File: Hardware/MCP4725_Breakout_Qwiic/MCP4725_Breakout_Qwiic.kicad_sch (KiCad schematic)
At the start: 24 parts, among them J1 Conn_01x02, J2 I2C, J3 Qwiic_RA, J4 Qwiic_RA, U2 MCP4725

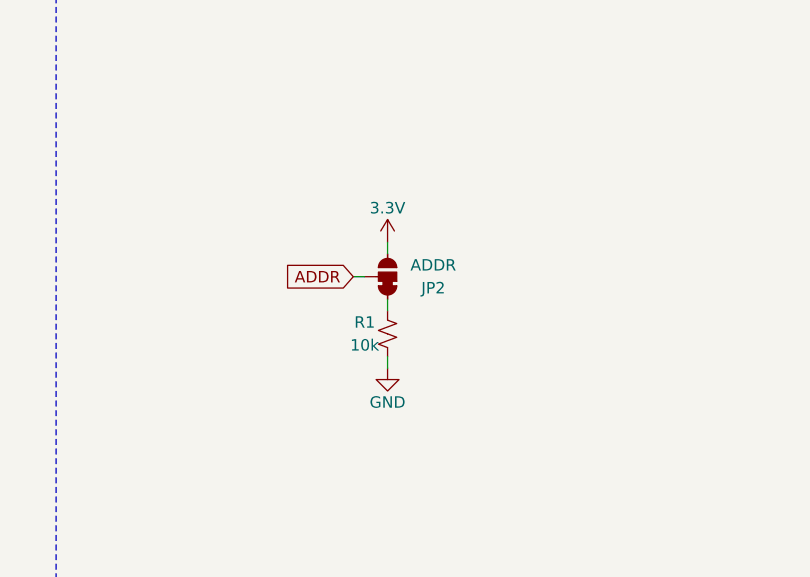
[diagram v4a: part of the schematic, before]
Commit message: Changes dual to single jumper
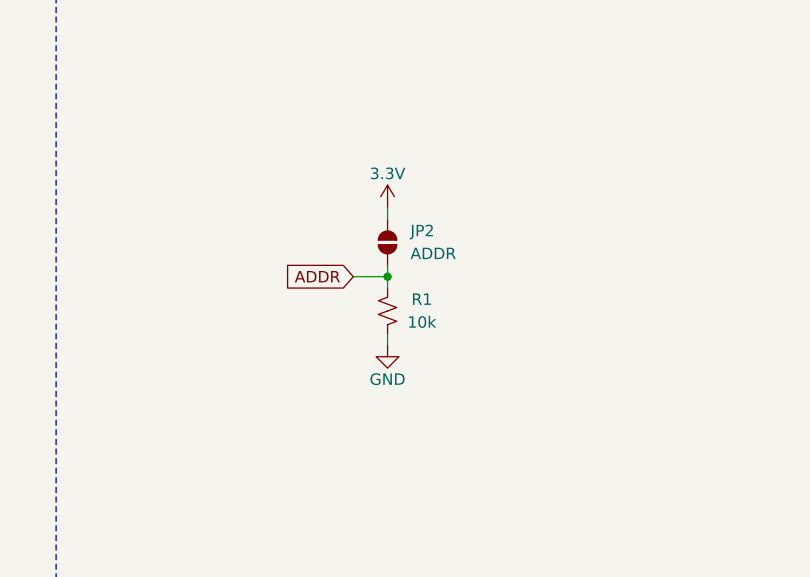
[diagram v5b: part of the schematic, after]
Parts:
- removed JP2: ADDR, SparkFun-Jumper:Jumper_3_NC-1_Trace, symbol SparkFun-Jumper:SolderJumper_3_Bridged12
- added JP2: ADDR, SparkFun-Jumper:Jumper_2_NO, symbol SparkFun-Jumper:SolderJumper_2_Open
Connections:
- net 3.3V: now also JP2.2 (B)
- net ADDR: now also R1.2, JP2.1 (A)
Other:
- moved on the sheet: R1
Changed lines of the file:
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@@
+	)
+	(junction
+		(at 139.7 132.08)
+		(diameter 0)
+		(color 0 0 0 0)
 	)
 	(junction
@@
 	(wire
 		(pts
-			(xy 135.89 132.08) (xy 137.16 132.08)
+			(xy 135.89 132.08) (xy 139.7 132.08)
 		)
 		(stroke
@@
 	(wire
 		(pts
-			(xy 139.7 128.27) (xy 139.7 129.54)
+			(xy 139.7 124.46) (xy 139.7 125.73)
 		)
 		(stroke
@@
 	(wire
 		(pts
-			(xy 139.7 142.24) (xy 139.7 140.97)
+			(xy 139.7 139.7) (xy 139.7 138.43)
 		)
 		(stroke
@@
 	(wire
 		(pts
-			(xy 139.7 134.62) (xy 139.7 135.89)
+			(xy 139.7 132.08) (xy 139.7 133.35)
+		)
+		(stroke
+			(width 0)
+			(type default)
+		)
+	)
+	(wire
+		(pts
+			(xy 139.7 130.81) (xy 139.7 132.08)
 		)
 		(stroke
@@
 		(row_heights 2.54 2.54 2.54 0 0 0 0 0 0 0 0)
 		(cells
-			(table_cell "Pin"
+			(table_cell "ADDR"
 				(exclude_from_sim no)
 				(at 124.46 102.87 0)
@@
 				)
 			)
-			(table_cell "GND"
+			(table_cell "Open"
 				(exclude_from_sim no)
 				(at 124.46 105.41 0)
@@
 				)
 			)
-			(table_cell "VDD"
+			(table_cell "Closed"
 				(exclude_from_sim no)
 				(at 124.46 107.95 0)
@@
 	)
 	(symbol
-		(lib_id "SparkFun-Jumper:SolderJumper_3_Bridged12")
-		(at 139.7 132.08 270)
-		(mirror x)
-		(unit 1)
-		(exclude_from_sim no)
-		(in_bom yes)
-		(on_board yes)
-		(dnp no)
-		(property "Reference" "JP2"
-			(at 144.78 133.35 90)
-			(effects
-				(font
-					(size 1.27 1.27)
-				)
-			)
-		)
-		(property "Value" "ADDR"
-			(at 144.78 130.81 90)
-			(effects
-				(font
-					(size 1.27 1.27)
-				)
-			)
-		)
-		(property "Footprint" "SparkFun-Jumper:Jumper_3_NC-1_Trace"
-			(at 134.62 132.08 0)
-			(effects
-				(font
-					(size 1.27 1.27)
-				)
-				(hide yes)
-			)
-		)
-		(property "Datasheet" "~"
-			(at 132.08 132.08 0)
-			(effects
-				(font
-					(size 1.27 1.27)
-				)
-				(hide yes)
-			)
-		)
-		(property "Description" "3-pole Solder Jumper, pins 1+2 closed/bridged"
-			(at 129.54 132.08 0)
-			(effects
-				(font
-					(size 1.27 1.27)
-				)
-				(hide yes)
-			)
-		)
-		(pin "2"
-		)
-		(pin "1"
-		)
-		(pin "3"
-		)
-		(instances
-			(project ""
-				(path "/bf35e96c-ec8b-4540-83a4-3cc6df170383"
-					(reference "JP2")
-					(unit 1)
-				)
-			)
-		)
-	)
-	(symbol
 		(lib_id "SparkFun-Aesthetic:Fiducial_0.5mm")
 		(at 278.13 175.26 0)
@@
 	)
 	(symbol
+		(lib_id "SparkFun-Jumper:SolderJumper_2_Open")
+		(at 139.7 128.27 90)
+		(unit 1)
+		(exclude_from_sim no)
+		(in_bom yes)
+		(on_board yes)
+		(dnp no)
+		(fields_autoplaced yes)
+		(property "Reference" "JP2"
+			(at 142.24 126.9999 90)
+			(effects
+				(font
+					(size 1.27 1.27)
+				)
+				(justify right)
+			)
+		)
+		(property "Value" "ADDR"
+			(at 142.24 129.5399 90)
+			(effects
+				(font
+					(size 1.27 1.27)
+				)
+				(justify right)
+			)
+		)
+		(property "Footprint" "SparkFun-Jumper:Jumper_2_NO"
+			(at 143.002 128.27 0)
+			(effects
+				(font
+					(size 1.27 1.27)
+				)
+				(hide yes)
+			)
+		)
+		(property "Datasheet" "~"
+			(at 146.05 128.27 0)
+			(effects
+				(font
+					(size 1.27 1.27)
+				)
+				(hide yes)
+			)
+		)
+		(property "Description" "Solder Jumper, 2-pole, open"
+			(at 148.59 128.27 0)
+			(effects
+				(font
+					(size 1.27 1.27)
+				)
+				(hide yes)
+			)
+		)
+		(pin "2"
+		)
+		(pin "1"
+		)
+		(instances
+			(project ""
+				(path "/bf35e96c-ec8b-4540-83a4-3cc6df170383"
+					(reference "JP2")
+					(unit 1)
+				)
+			)
+		)
+	)
+	(symbol
 		(lib_id "SparkFun-Resistor:10k_0603")
-		(at 139.7 138.43 90)
+		(at 139.7 135.89 270)
+		(mirror x)
 		(unit 1)
 		(exclude_from_sim no)
@@
 		(dnp no)
 		(property "Reference" "R1"
-			(at 137.16 137.16 90)
+			(at 143.51 134.62 90)
 			(effects
 				(font
@@
 		)
 		(property "Value" "10k"
-			(at 137.16 139.7 90)
+			(at 143.51 137.16 90)
 			(effects
 				(font
@@
 		)
 		(property "Footprint" "SparkFun-Resistor:R_0603_1608Metric"
-			(at 144.018 138.43 0)
+			(at 135.382 135.89 0)
 			(effects
 				(font
@@
 		)
 		(property "Datasheet" "https://www.vishay.com/docs/20035/dcrcwe3.pdf"
-			(at 148.59 138.43 0)
+			(at 130.81 135.89 0)
 			(effects
 				(font
@@
 		)
 		(property "Description" "Resistor"
-			(at 151.13 138.43 0)
+			(at 128.27 135.89 0)
 			(effects
 				(font
@@
 		)
 		(property "PROD_ID" "RES-00824"
-			(at 146.05 138.43 0)
+			(at 133.35 135.89 0)
 			(effects
 				(font
@@
 	(symbol
 		(lib_id "SparkFun-PowerSymbol:GND")
-		(at 139.7 142.24 0)
+		(at 139.7 139.7 0)
 		(unit 1)
 		(exclude_from_sim no)
@@
 		(fields_autoplaced yes)
 		(property "Reference" "#PWR02"
+			(at 139.7 146.05 0)
+			(effects
+				(font
+					(size 1.27 1.27)
+				)
+				(hide yes)
+			)
+		)
+		(property "Value" "GND"
+			(at 139.7 143.51 0)
+			(do_not_autoplace yes)
+			(effects
+				(font
+					(size 1.27 1.27)
+				)
+			)
+		)
+		(property "Footprint" ""
+			(at 139.7 139.7 0)
+			(effects
+				(font
+					(size 1.27 1.27)
+				)
+				(hide yes)
+			)
+		)
+		(property "Datasheet" ""
+			(at 139.7 139.7 0)
+			(effects
+				(font
+					(size 1.27 1.27)
+				)
+				(hide yes)
+			)
+		)
+		(property "Description" "Power symbol creates a global label with name \"GND\" , ground"
 			(at 139.7 148.59 0)
-			(effects
-				(font
-					(size 1.27 1.27)
-				)
-				(hide yes)
-			)
-		)
-		(property "Value" "GND"
-			(at 139.7 146.05 0)
-			(do_not_autoplace yes)
-			(effects
-				(font
-					(size 1.27 1.27)
-				)
-			)
-		)
-		(property "Footprint" ""
-			(at 139.7 142.24 0)
-			(effects
-				(font
-					(size 1.27 1.27)
-				)
-				(hide yes)
-			)
-		)
-		(property "Datasheet" ""
-			(at 139.7 142.24 0)
-			(effects
-				(font
-					(size 1.27 1.27)
-				)
-				(hide yes)
-			)
-		)
-		(property "Description" "Power symbol creates a global label with name \"GND\" , ground"
-			(at 139.7 151.13 0)
 			(effects
 				(font
@@
 	(symbol
 		(lib_id "SparkFun-PowerSymbol:3.3V")
-		(at 139.7 128.27 0)
+		(at 139.7 124.46 0)
 		(unit 1)
 		(exclude_from_sim no)
@@
 		(fields_autoplaced yes)
 		(property "Reference" "#PWR03"
-			(at 139.7 132.08 0)
+			(at 139.7 128.27 0)
 			(effects
 				(font
@@
 		)
 		(property "Value" "3.3V"
+			(at 139.7 120.65 0)
+			(do_not_autoplace yes)
+			(effects
+				(font
+					(size 1.27 1.27)
+				)
+			)
+		)
+		(property "Footprint" ""
 			(at 139.7 124.46 0)
-			(do_not_autoplace yes)
-			(effects
-				(font
-					(size 1.27 1.27)
-				)
-			)
-		)
-		(property "Footprint" ""
-			(at 139.7 128.27 0)
 			(effects
 				(font
@@
 		)
 		(property "Datasheet" ""
-			(at 139.7 128.27 0)
+			(at 139.7 124.46 0)
 			(effects
 				(font
@@
 		)
 		(property "Description" "Power symbol creates a global label with name \"3.3V\""
-			(at 139.7 134.62 0)
-			(effects
-				(font
+			(at 139.7 130.81 0)
+			(effects
+				(font

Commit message: Fixes jumpers on more time
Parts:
- removed JP2: ADDR, SparkFun-Jumper:Jumper_2_NO, symbol SparkFun-Jumper:SolderJumper_2_Open
- added JP2: ADDR, SparkFun-Jumper:Jumper_2_NC_Trace, symbol SparkFun-Jumper:SolderJumper_2_Bridged
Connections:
- net 3.3V: now also R1.2
- net ADDR: now also R1.1, JP2.2 (B); no longer R1.2
- net GND: now also JP2.1 (A); no longer R1.1
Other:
- moved on the sheet: R1

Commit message: Adds gerbers
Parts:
- U2: PROD_ID (none) -> IC-08886
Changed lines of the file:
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@@
 			)
 		)
-		(property "PROD_ID" ""
+		(property "PROD_ID" "IC-08886"
 			(at 86.36 57.15 0)
 			(effects
